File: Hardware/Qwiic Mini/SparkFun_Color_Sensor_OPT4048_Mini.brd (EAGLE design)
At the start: 25.4 x 12.7 mm, 51 parts, among them J4 QWIIC_RIGHT_ANGLE, J5 QWIIC_RIGHT_ANGLE, U1 OPT4048

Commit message: Approves some DRC errors
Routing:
- net ADDR: track 10.9 -> 10.3 mm
- net 3.3V: vias 6 -> 5
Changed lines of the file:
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@@
 <wire x1="21.8186" y1="6.35" x2="22.3012" y2="6.8326" width="0.4064" layer="16"/>
 <wire x1="8.89" y1="9.31" x2="10.414" y2="9.31" width="0.4064" layer="1"/>
-<via x="10.16" y="4.4196" extent="1-16" drill="0.3048"/>
 <wire x1="10.16" y1="5.461" x2="10.16" y2="4.4196" width="0.4064" layer="16"/>
 <wire x1="8.89" y1="9.017" x2="8.89" y2="9.31" width="0.4064" layer="1"/>
@@
 <contactref element="0X45" pad="1"/>
 <contactref element="0X46" pad="1"/>
-<wire x1="6.4135" y1="4.1148" x2="6.4135" y2="4.7498" width="0.1524" layer="16"/>
 <wire x1="6.4135" y1="4.7498" x2="6.2992" y2="4.8641" width="0.1524" layer="16"/>
 <wire x1="6.2992" y1="4.8641" x2="6.2992" y2="5.8166" width="0.1524" layer="16"/>

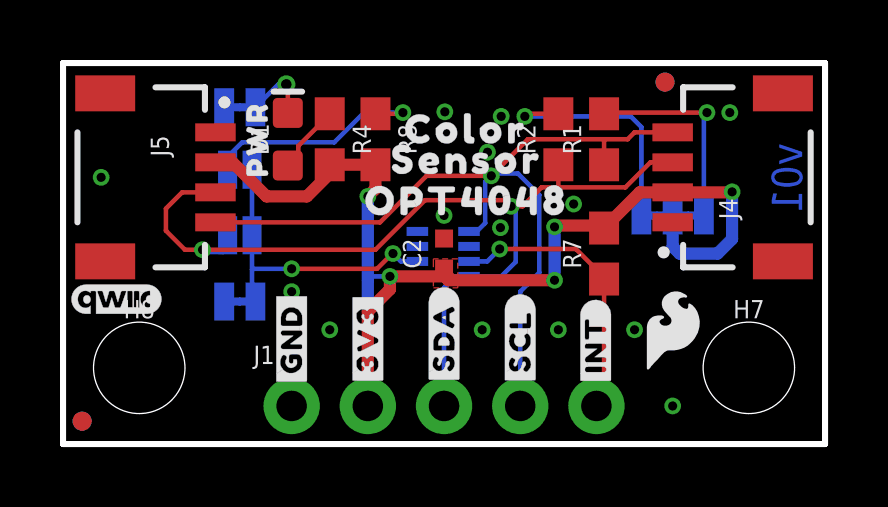
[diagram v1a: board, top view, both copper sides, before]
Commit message: Fixes some traces
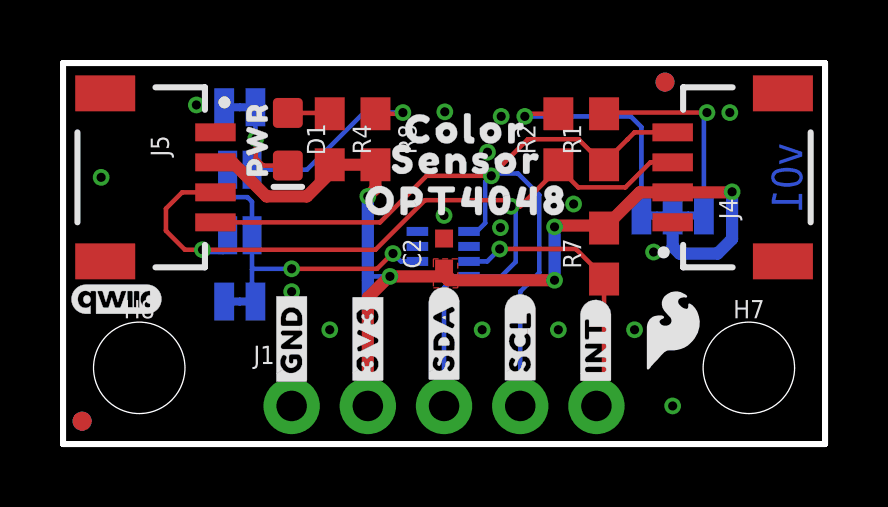
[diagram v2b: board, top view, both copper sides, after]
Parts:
- turned 0X45 to 180 degrees
- turned D1 to 270 degrees
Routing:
- net N$9: track 7.81 -> 6.75 mm
- net N$3: track 2.31 -> 1.45 mm
- net ADDR: track 10.3 -> 10.9 mm
- net N$4: track 2.32 -> 2.87 mm

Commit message: Adds correct red LEDs and their resistors, updates PROD_ID for part.
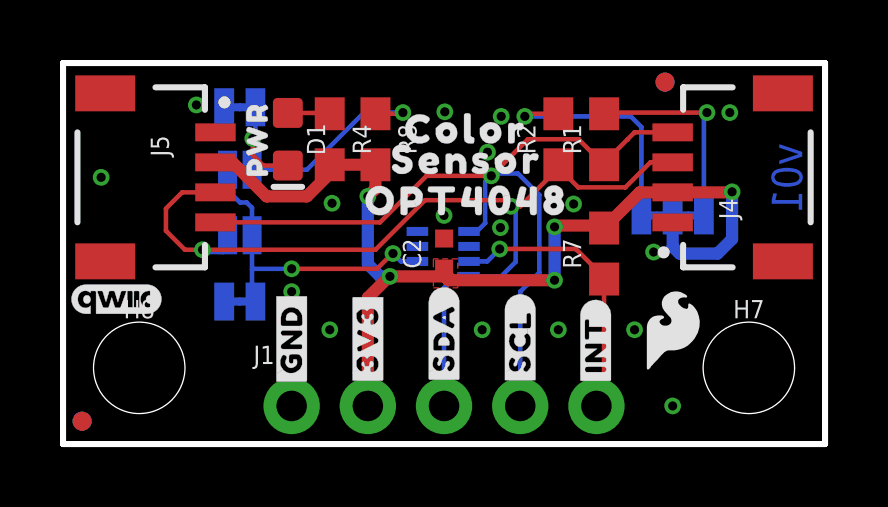
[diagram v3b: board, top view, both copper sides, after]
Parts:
- R4: value 1k -> 4.7k
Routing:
- net 3.3V: track 36.6 -> 35.1 mm
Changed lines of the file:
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@@
 <drawing>
 <settings>
-<setting alwaysvectorfont="yes"/>
+<setting alwaysvectorfont="no"/>
 <setting verticaltext="up"/>
 </settings>
@@
 <element name="D1" library="SparkFun-LED" package="LED-0603" value="RED" x="7.493" y="10.16" smashed="yes" rot="R270">
 <attribute name="NAME" x="8.128" y="10.16" size="0.6096" layer="25" font="vector" ratio="20" rot="R270" align="bottom-center"/>
-<attribute name="PROD_ID" value="DIO-00819" x="22.733" y="22.86" size="1.778" layer="27" rot="R270" display="off"/>
-<attribute name="VALUE" x="6.858" y="10.16" size="0.6096" layer="27" font="vector" ratio="20" rot="R270" align="top-center"/>
-</element>
-<element name="R4" library="SparkFun-Resistors" package="0603" value="1k" x="8.89" y="10.16" smashed="yes" rot="R270">
+<attribute name="PROD_ID" value="DIO-17976" x="22.733" y="22.86" size="1.778" layer="27" rot="R270" display="off"/>
+</element>
+<element name="R4" library="SparkFun-Resistors" package="0603" value="4.7k" x="8.89" y="10.16" smashed="yes" rot="R270">
 <attribute name="NAME" x="9.652" y="10.16" size="0.6096" layer="25" font="vector" ratio="20" rot="R270" align="bottom-center"/>
-<attribute name="PROD_ID" value="RES-07856" x="16.51" y="26.67" size="1.778" layer="27" rot="R270" display="off"/>
-<attribute name="VALUE" x="8.128" y="10.16" size="0.6096" layer="27" font="vector" ratio="20" rot="R270" align="top-center"/>
+<attribute name="PROD_ID" value="RES-07857" x="16.51" y="26.67" size="1.778" layer="27" rot="R270" display="off"/>
+<attribute name="VALUE" value="4.7k" x="8.128" y="10.16" size="0.6096" layer="27" font="vector" ratio="20" rot="R270" align="top-center"/>
 </element>
 <element name="LED" library="SparkFun-Jumpers" package="SMT-JUMPER_2_NC_TRACE_SILK" package3d_urn="urn:adsk.eagle:package:39281/1" value="JUMPER-SMT_2_NC_TRACE_SILK" x="5.8928" y="11.2268" smashed="yes" rot="MR180">
@@
 <via x="4.445" y="11.303" extent="1-16" drill="0.3048"/>
 <via x="19.685" y="6.4008" extent="1-16" drill="0.3048"/>
+<via x="8.9662" y="8.0264" extent="1-16" drill="0.3048"/>
 </signal>
 <signal name="3.3V">
@@
 <via x="10.16" y="8.255" extent="1-16" drill="0.3048"/>
 <wire x1="10.16" y1="1.27" x2="10.16" y2="4.8768" width="0.4064" layer="1"/>
-<wire x1="10.16" y1="8.255" x2="10.16" y2="5.461" width="0.4064" layer="16"/>
 <wire x1="18.034" y1="7.2" x2="18.117" y2="7.283" width="0.4064" layer="1"/>
 <wire x1="18.117" y1="7.283" x2="19.224" y2="8.39" width="0.4064" layer="1"/>
@@
 <wire x1="16.383" y1="7.239" x2="16.427" y2="7.283" width="0.4064" layer="1"/>
 <wire x1="16.427" y1="7.283" x2="18.117" y2="7.283" width="0.4064" layer="1"/>
-<wire x1="11.811" y1="5.588" x2="10.8966" y2="5.588" width="0.1524" layer="16"/>
-<wire x1="10.8966" y1="5.588" x2="10.287" y2="5.588" width="0.1524" layer="16"/>
-<wire x1="10.287" y1="5.588" x2="10.16" y2="5.461" width="0.1524" layer="16"/>
 <wire x1="20.32" y1="8.39" x2="22.2838" y2="8.39" width="0.4064" layer="1"/>
 <wire x1="22.2838" y1="8.39" x2="22.3012" y2="8.4074" width="0.4064" layer="1"/>
@@
 <wire x1="21.8186" y1="6.35" x2="22.3012" y2="6.8326" width="0.4064" layer="16"/>
 <wire x1="8.89" y1="9.31" x2="10.414" y2="9.31" width="0.4064" layer="1"/>
-<wire x1="10.16" y1="5.461" x2="10.16" y2="4.4196" width="0.4064" layer="16"/>
 <wire x1="8.89" y1="9.017" x2="8.89" y2="9.31" width="0.4064" layer="1"/>
 <via x="10.8966" y="5.588" extent="1-16" drill="0.3048"/>
@@
 <wire x1="10.8966" y1="5.588" x2="12.835" y2="5.588" width="0.4064" layer="1"/>
 <wire x1="12.835" y1="5.588" x2="12.835" y2="5.461" width="0.4064" layer="1"/>
+<wire x1="10.8966" y1="5.588" x2="10.5664" y2="5.588" width="0.4064" layer="16"/>
+<wire x1="11.811" y1="5.588" x2="10.8966" y2="5.588" width="0.3048" layer="16"/>
+<wire x1="10.5664" y1="5.588" x2="10.16" y2="5.9944" width="0.4064" layer="16"/>
+<wire x1="10.16" y1="5.9944" x2="10.16" y2="8.255" width="0.4064" layer="16"/>
 </signal>
 <signal name="SCL">
@@
 <wire x1="7.62" y1="5.842" x2="6.3246" y2="5.842" width="0.1524" layer="16"/>
 <wire x1="6.3246" y1="5.842" x2="6.2992" y2="5.8166" width="0.1524" layer="16"/>
-<wire x1="6.2992" y1="6.9596" x2="6.2992" y2="8.0772" width="0.1524" layer="16"/>
-<wire x1="5.71973125" y1="8.2296" x2="5.4864" y2="8.46293125" width="0.1524" layer="16"/>
+<wire x1="6.2992" y1="6.9596" x2="6.2992" y2="7.874" width="0.1524" layer="16"/>
+<wire x1="5.89753125" y1="8.0518" x2="5.4864" y2="8.46293125" width="0.1524" layer="16"/>
 <wire x1="5.4864" y1="8.46293125" x2="5.4864" y2="9.144" width="0.1524" layer="16"/>
-<wire x1="6.2992" y1="8.0772" x2="6.1468" y2="8.2296" width="0.1524" layer="16"/>
-<wire x1="6.1468" y1="8.2296" x2="5.71973125" y2="8.2296" width="0.1524" layer="16"/>
+<wire x1="6.2992" y1="7.874" x2="6.1214" y2="8.0518" width="0.1524" layer="16"/>
+<wire x1="6.1214" y1="8.0518" x2="5.89753125" y2="8.0518" width="0.1524" layer="16"/>
 </signal>
 <signal name="N$1">
@@
 <contactref element="R4" pad="1"/>
 <contactref element="D1" pad="A"/>
-<wire x1="8.89" y1="11.01" x2="8.89" y2="10.9848" width="0.1524" layer="1"/>
 <wire x1="8.89" y1="11.037" x2="8.89" y2="11.01" width="0.4064" layer="1"/>
 <wire x1="7.493" y1="11.037" x2="8.89" y2="11.037" width="0.1524" layer="1"/>
@@
 <contactref element="D1" pad="C"/>
 <contactref element="LED" pad="2"/>
-<wire x1="6.4135" y1="11.2268" x2="6.4135" y2="10.1981" width="0.1524" layer="16"/>
-<wire x1="6.4135" y1="10.1981" x2="6.4262" y2="10.1854" width="0.1524" layer="16"/>
-<via x="6.4262" y="10.1854" extent="1-16" drill="0.3048"/>
-<wire x1="6.4262" y1="10.1854" x2="6.4262" y2="9.525" width="0.1524" layer="1"/>
+<wire x1="6.4135" y1="11.2268" x2="6.4135" y2="10.2743" width="0.1524" layer="16"/>
+<wire x1="6.4135" y1="10.2743" x2="6.3246" y2="10.1854" width="0.1524" layer="16"/>
+<via x="6.3246" y="10.1854" extent="1-16" drill="0.3048"/>
+<wire x1="6.3246" y1="10.1854" x2="6.3246" y2="9.6266" width="0.1524" layer="1"/>
 <wire x1="7.493" y1="9.283" x2="6.6682" y2="9.283" width="0.1524" layer="1"/>
-<wire x1="6.6682" y1="9.283" x2="6.4262" y2="9.525" width="0.1524" layer="1"/>
+<wire x1="6.6682" y1="9.283" x2="6.3246" y2="9.6266" width="0.1524" layer="1"/>
 </signal>
 <signal name="N$9">
